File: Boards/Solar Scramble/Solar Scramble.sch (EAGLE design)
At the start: 18 parts

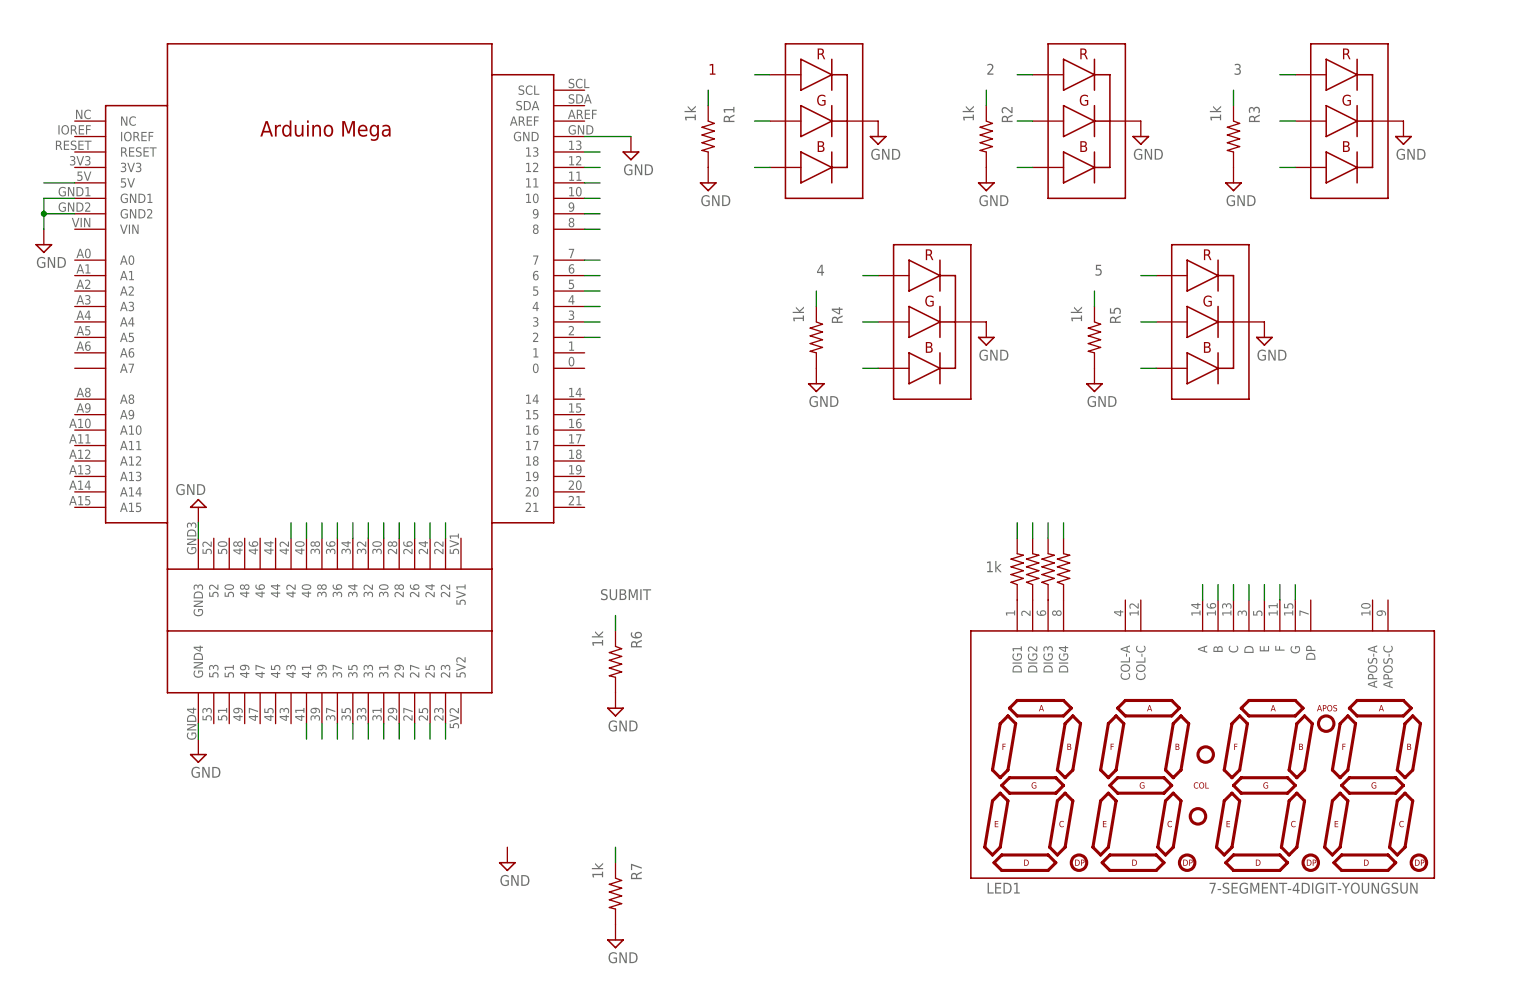
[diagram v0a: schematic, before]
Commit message: Finish solar scramble
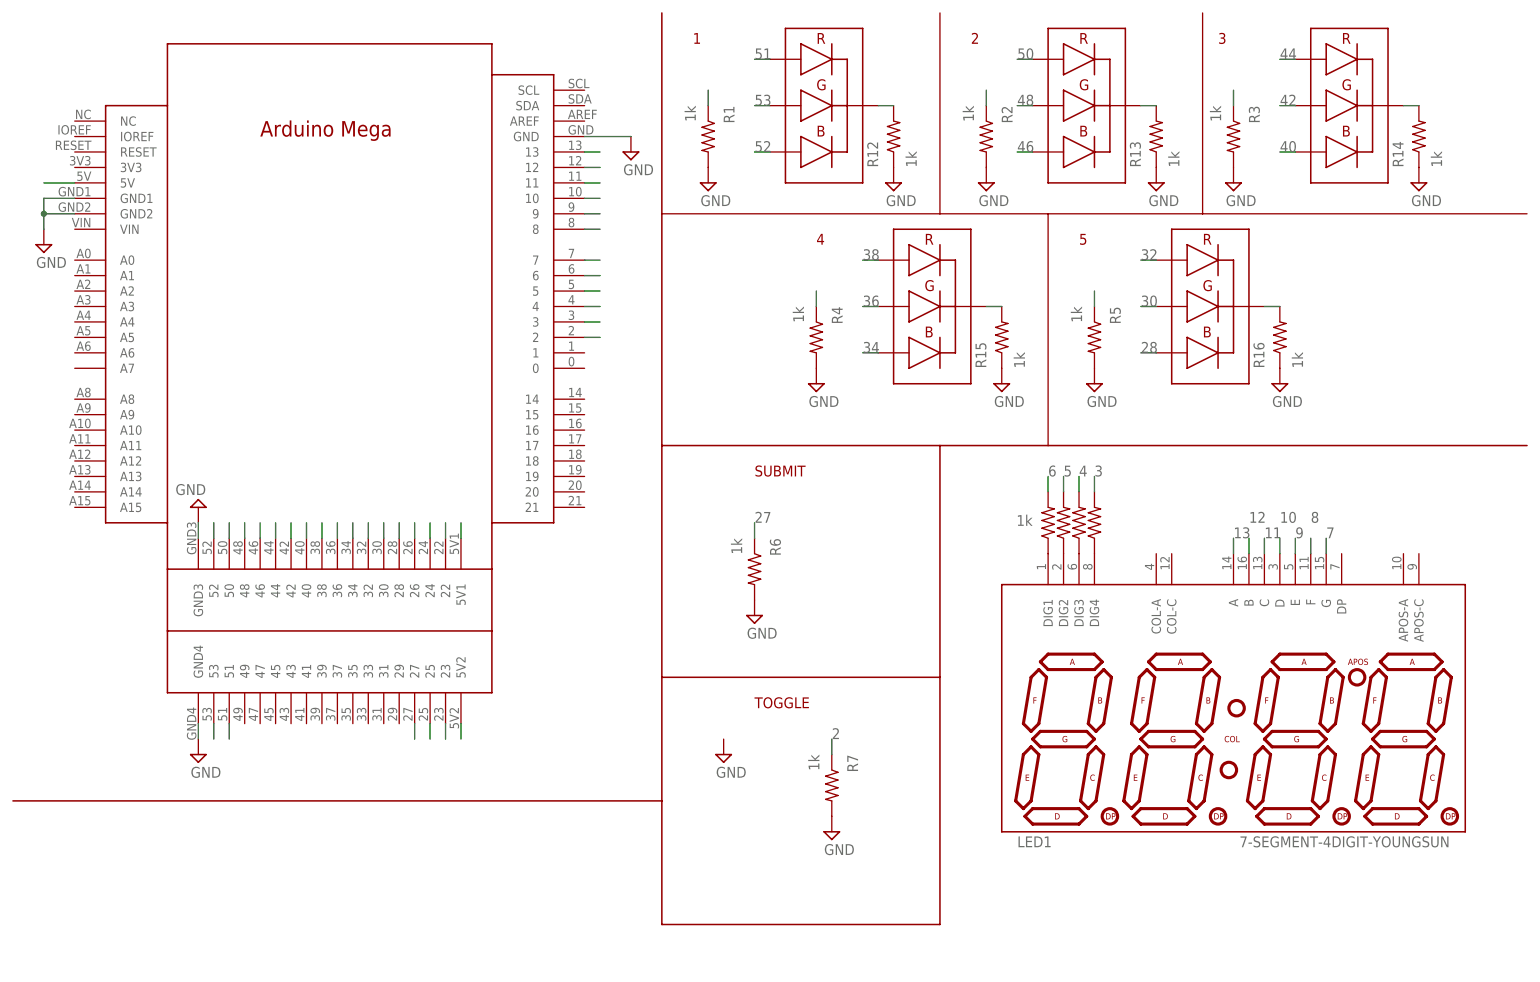
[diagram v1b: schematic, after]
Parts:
- added R12, R13, R14, R15, R16: 1k, pie:R-US_R0603
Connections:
- removed net 29: U$1.29, U$2.G
- removed net 31: U$1.31, U$6.R
- removed net 33: U$1.33, U$6.B
- removed net 35: U$1.35, U$3.G
- removed net 37: U$1.37, U$4.R
- removed net 39: U$1.39, U$4.B
- removed net 41: U$1.41, U$5.G
- new net 44: U$1.44, U$3.R
- new net 46: U$1.46, U$6.B
- new net 48: U$1.48, U$6.G
- new net 50: U$1.50, U$6.R
- new net 51: U$1.51, U$2.R
- new net 52: U$1.52, U$2.B
- new net 53: U$1.53, U$2.G
- new net N$1: R15.2, U$4.CAT
- new net N$2: R12.2, U$2.CAT
- new net N$7: R13.2, U$6.CAT
- new net N$8: R14.2, U$3.CAT
- new net N$9: R16.2, U$5.CAT
- net 28: now also U$5.B; no longer U$2.R
- net 30: now also U$5.G; no longer U$2.B
- net 32: now also U$5.R; no longer U$6.G
- net 34: now also U$4.B; no longer U$3.R
- net 36: now also U$4.G; no longer U$3.B
- net 38: now also U$4.R; no longer U$4.G
- net 40: now also U$3.B; no longer U$5.R
- net 42: now also U$3.G; no longer U$5.B
- net 5V: now also U$1.5V1, U$1.5V2
- net GND: now also R12.1, R13.1, R14.1, R15.1, R16.1; no longer U$2.CAT, U$3.CAT, U$4.CAT, U$5.CAT, U$6.CAT
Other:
- note added: "TOGGLE"
- moved on the sheet: LED1, R6, R7

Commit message: Make some changes
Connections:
- net 5V: no longer U$1.5V
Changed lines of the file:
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@@
 <drawing>
 <settings>
-<setting alwaysvectorfont="no"/>
+<setting alwaysvectorfont="yes"/>
 <setting verticaltext="up"/>
 </settings>
@@
 <net name="5V" class="0">
 <segment>
-<pinref part="U$1" gate="G$1" pin="5V"/>
-<wire x1="10.16" y1="157.48" x2="5.08" y2="157.48" width="0.1524" layer="91"/>
-</segment>
-<segment>
 <pinref part="U$1" gate="G$1" pin="5V1"/>
